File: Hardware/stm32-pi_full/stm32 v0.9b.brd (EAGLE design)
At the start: 131.4 x 105.8 mm, 272 parts, among them J1 SOLDERJUMPERNO, J2 5-1814400-1, U1 ESP32-WROOM-32D, Y1 6MM_3.5MM_CRYSTAL

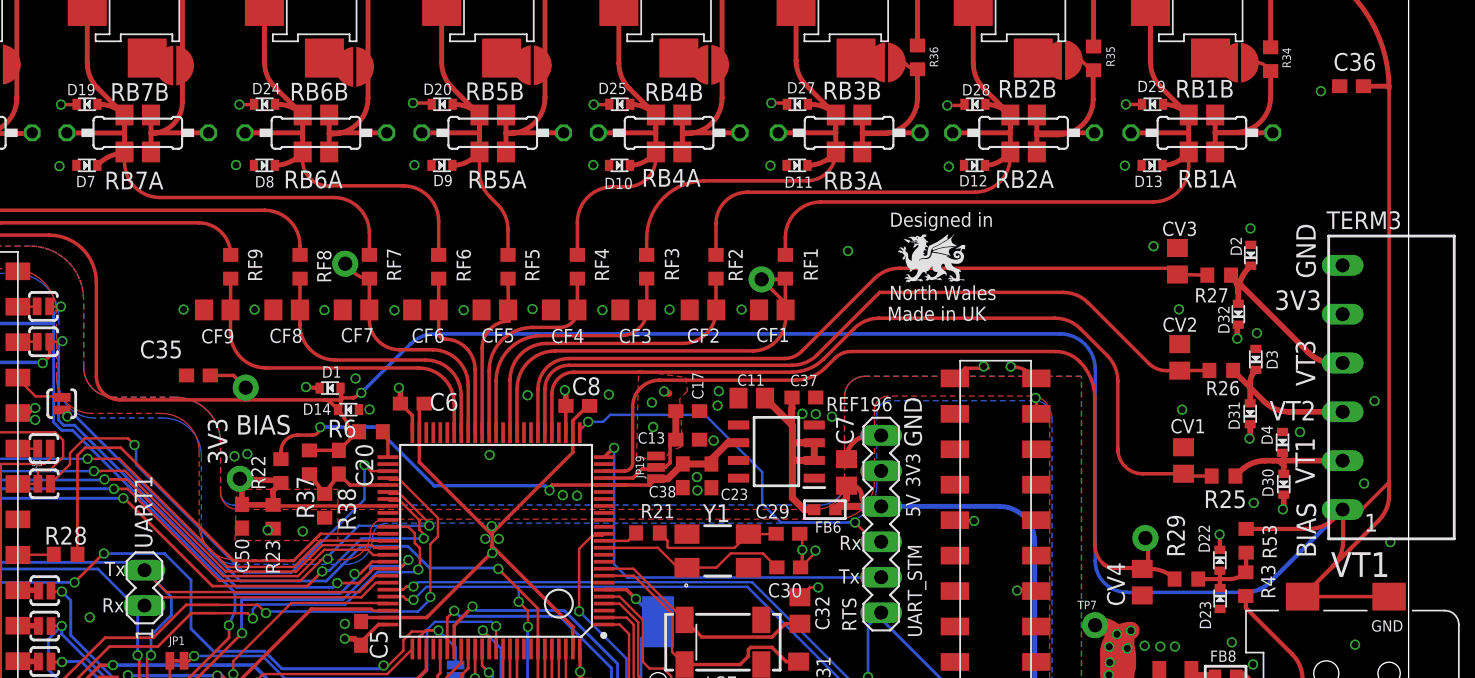
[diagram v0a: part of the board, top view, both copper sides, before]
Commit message: bias changed to inverting op-amp with in-the-loop compensator
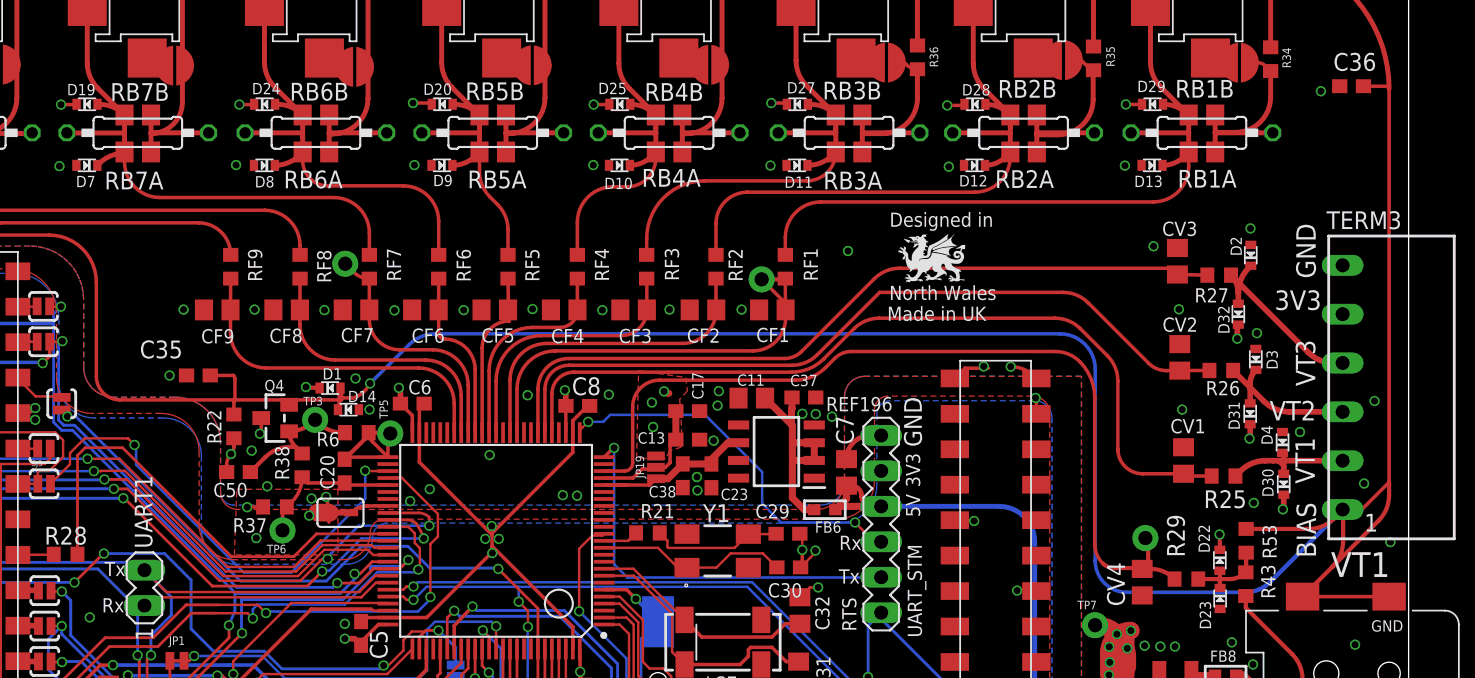
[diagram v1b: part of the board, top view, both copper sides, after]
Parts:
- removed R23: 10k, resistor:R0603
- removed TP10: TEST-POINTPOGO_PTH, SparkFun-Connectors:1X01_NO_SILK
- added Q4: (no value), microbuilder:SOT23-WIDE
- added SJ1: (no value), jumper-con_db:SJ-CON
- added TP3, TP6: TEST-POINTPOGO_PTH, SparkFun-Connectors:1X01_NO_SILK
- C20: value 2.2uF -> 2nF
- C50: value (none) -> 1nF
- R22: value 10k -> 1k
- R37: value 0R -> 1k
- R6: value 0R -> 5R
- moved TP5 10.9 mm to (58.4, 64.1)
- moved R22 4.65 mm to (47.2, 64.6)
- moved R37 4.04 mm to (50.2, 58.8), turned to 0 degrees
- moved R38 3.32 mm to (52.1, 61.8)
- moved C50 3.18 mm to (47.5, 61.3), turned to 180 degrees
- moved R6 1.02 mm to (56.0, 64.1), turned to 180 degrees
- moved C20 0.76 mm to (55.1, 61.4), turned to 90 degrees
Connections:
- removed net BIAS_: R6.2, STM32F303VE.51
- removed net BIAS_IN: C50.2, R22.1, R23.2, STM32F303VE.58, TP10.1
- new net OPAMP_FB2: C50.1, Q4.1, R38.1, R6.2, TP3.1
- new net OPAMP_NON-INVERT+: SJ1.1, STM32F303VE.58
- new net OPAMP_OUT: C20.2, R6.1, STM32F303VE.51, TP5.1
- net +3V3ANA: now also Q4.3, R37.1
- net AGND: now also C50.2, R22.1, SJ1.2; no longer C50.1, R23.1, R38.2
- net BIAS: now also Q4.2, R22.2; no longer C20.1, R37.1, R6.1, TP5.1
- net LED2: now also STM32F303VE.59; no longer STM32F303VE.56
- net LED3: now also STM32F303VE.60; no longer STM32F303VE.57
- net OPAMP_INVERT-: now also C20.1, R38.2, TP6.1; no longer C20.2, R38.1
- net VREF+: no longer R22.2
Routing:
- net VREF+: track 44.2 -> 12.7 mm, vias 2 -> 0
- net BIAS_IN: track 17.3 -> 0.00 mm
- net OPAMP_OUT: track 0.00 -> 11.3 mm
- net OPAMP_FB2: track 0.00 -> 10.1 mm
- net BIAS: track 577.6 -> 570.6 mm
- net AGND: track 15.5 -> 21.4 mm, vias 85 -> 91
- net OPAMP_INVERT-: track 7.39 -> 10.5 mm
- net OPAMP_NON-INVERT+: track 0.00 -> 2.74 mm
- net +3V3ANA: track 72.6 -> 74.9 mm, vias 23 -> 25
- net BIAS_: track 1.97 -> 0.00 mm
- net RPI_PWR: track 35.1 -> 33.5 mm
- net LED3: track 73.8 -> 73.0 mm
- net BUTTON1_STM: track 35.6 -> 35.0 mm

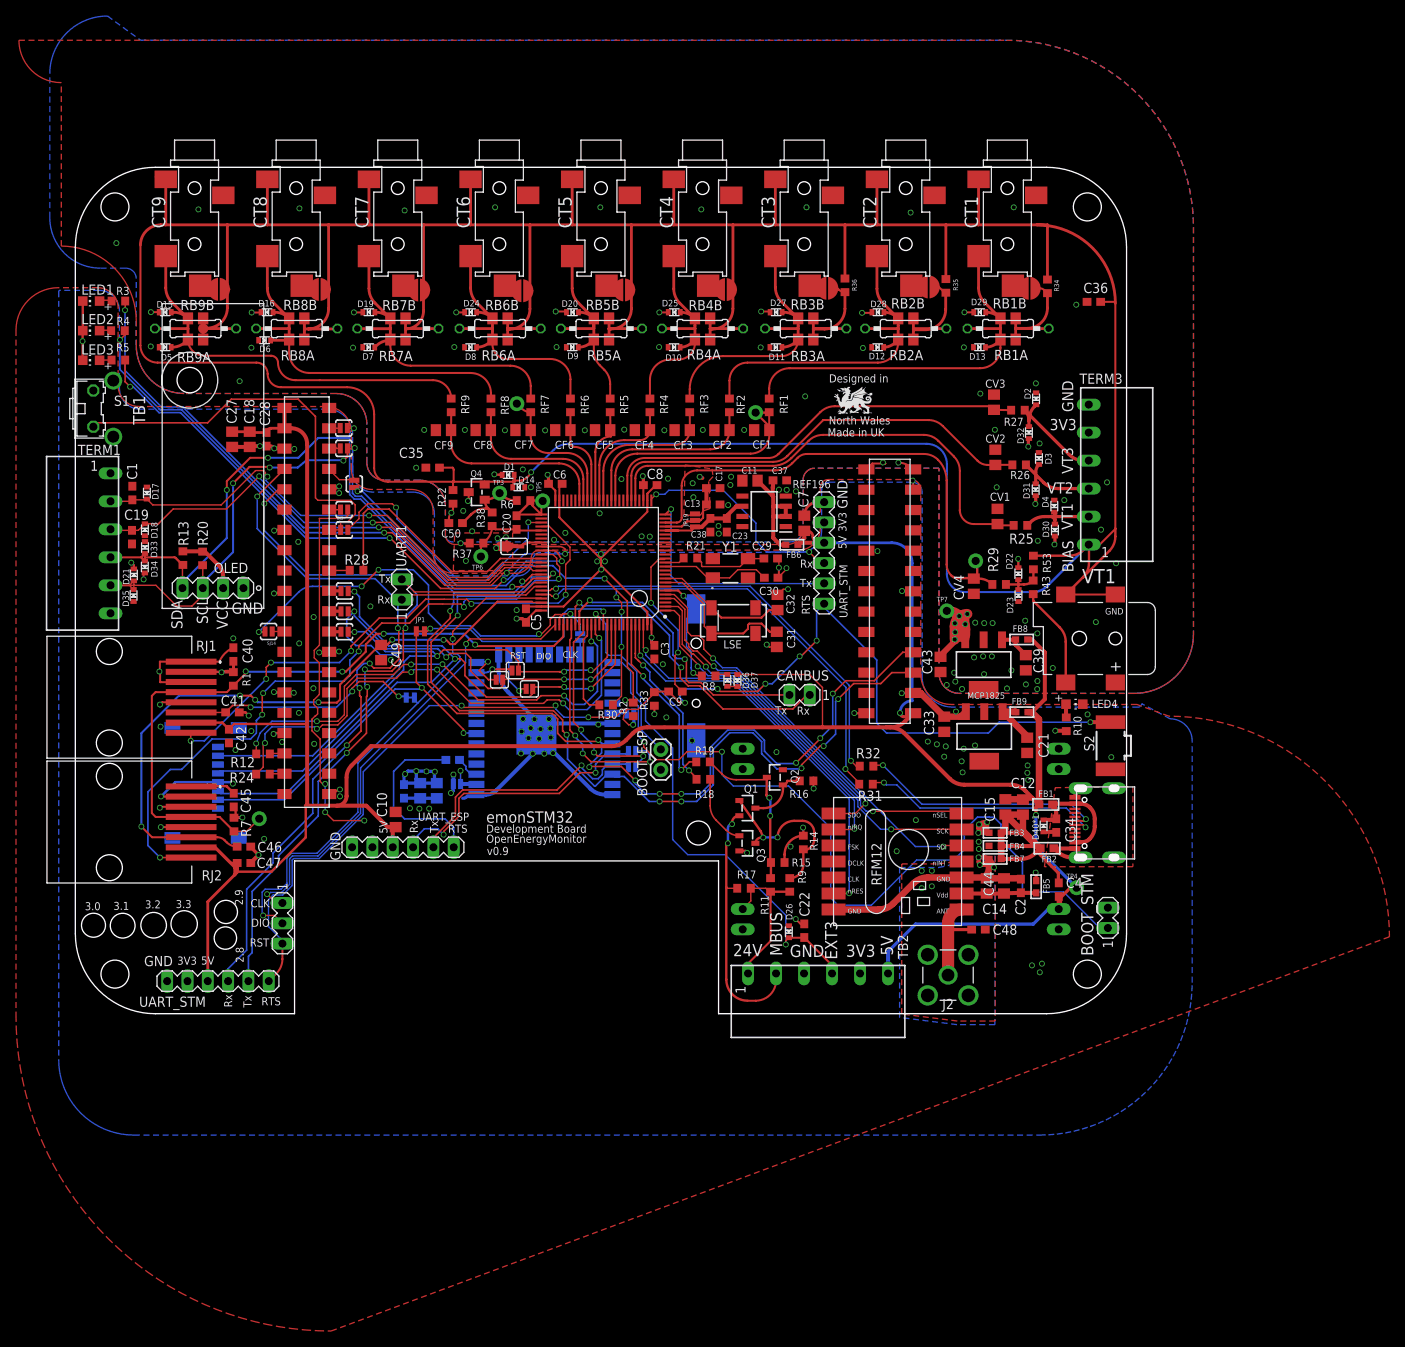
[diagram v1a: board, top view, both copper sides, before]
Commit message: update readme.md
including link for the enclosure CAD
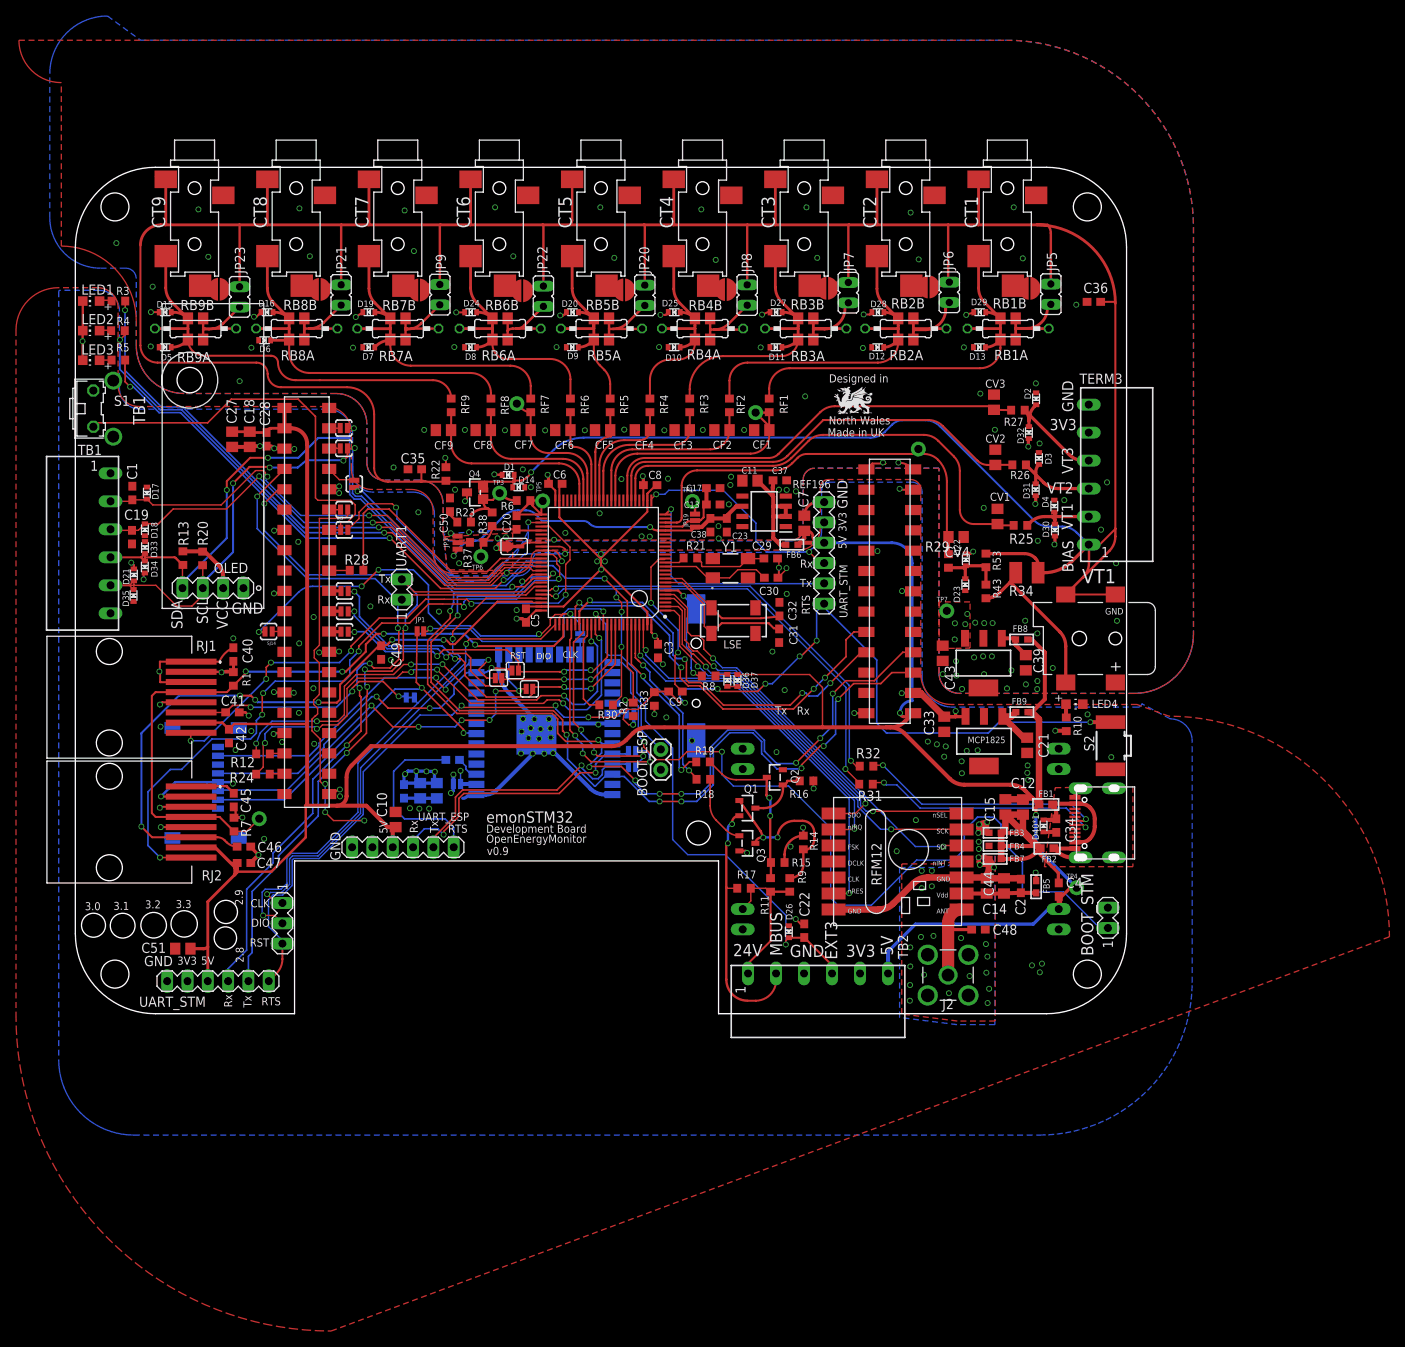
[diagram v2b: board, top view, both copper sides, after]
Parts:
- removed CANBUS: TX/RX, con-lstb-db:MA02-1
- removed R35, R36: 0R, rcl:R0603
- added C51: 22uF, rcl:C0805
- added JP2: JUMPER-SMT_2_NO_NO-SILK, SparkFun-Jumpers:SMT-JUMPER_2_NO_NO-SILK
- added JP20, JP21, JP22, JP23, JP5, JP6, JP7, JP8, JP9: (no value), jumper-con_db:JP1
- added JP3: JUMPER-SMT_3_NO_NO-SILK, SparkFun-Jumpers:SMT-JUMPER_3_NO_NO-SILK
- added R23: 1k, resistor:R0603
- added TP1: TEST-POINTPOGO_PTH, SparkFun-Connectors:1X01_NO_SILK
- C20: value 2nF -> 2.2nF
- C31, C32: device rcl:C0805 -> rcl:C0603
- C48: value 100nF -> (none)
- C49: value 10pF -> 1nF; device rcl:C0805 -> rcl:C0603
- C50: value 1nF -> 1uf
- C7: value 2.2uF -> 22uF
- CF1, CF2, CF3, CF4, CF5, CF6, CF7, CF8, CF9, CV1, CV2, CV3, CV4: value 10nF -> 10nF 5%
- JP1: value JUMPER-SMT_2_NC_TRACE_NO-SILK -> JUMPER-SMT_2_NO_NO-SILK; device SparkFun-Jumpers:SMT-JUMPER_2_NC_TRACE_NO-SILK -> SparkFun-Jumpers:SMT-JUMPER_2_NO_NO-SILK
- PS1: value LT1461AIS8-3.3#PBF -> REF191ESZ
- R22: value 1k -> 10k
- R25, R26, R27: value 9k1 -> 9k1 0.1%
- R34: value 0R -> (none); device rcl:R0603 -> rcl:R1210
- R37: value 1k -> 2k
- R6: value 5R -> 20R
- RB1A, RB1B: value 22r 0.3W 1% -> 22r
- RB1_: value 22r 0.5W -> (none)
- RB2_, RB3_, RB4_, RB5_, RB6_, RB7_, RB8_: value 22r -> (none)
- RB9A, RB9B: value 100R 0.1% -> 22r
- RB9_: value 100R 0.1% -> (none)
- moved R34 35.9 mm to (118.9, 55.1), turned to 0 degrees
- moved TP20 15.7 mm to (105.4, 70.6)
- moved R29 6.99 mm to (109.1, 56.6), turned to 90 degrees
- moved D22 6.79 mm to (111.3, 56.7)
- moved D23 6.79 mm to (111.2, 53.6)
- moved CV4 6.54 mm to (110.1, 59.6), turned to 0 degrees
- moved R53 5.94 mm to (113.8, 56.7)
- moved R43 5.93 mm to (113.8, 52.8)
- moved R22 3.00 mm to (46.3, 67.5), turned to 270 degrees
- moved C50 2.40 mm to (46.8, 63.6), turned to 90 degrees
- moved C35 2.24 mm to (42.4, 68.1)
- moved C43 1.42 mm to (108.4, 45.1)
- moved C32 0.87 mm to (88.0, 50.6)
- moved MCP1825 0.60 mm to (113.6, 34.1)
- moved C31 0.54 mm to (88.0, 47.2)
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- renumbered TERM1 to TB1
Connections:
- removed net IO3_EX: EXPANSION.17
- removed net IO5_EX: EXPANSION.19
- removed net N$28: JP14.1, R36.1, RB3A.2, RB3B.2, RB3_.2
- new net N$12: JP3.2, R37.1
- new net N$24: JP20.2, RB5A.2, RB5B.2, RB5_.2
- new net N$25: JP22.2, RB6A.2, RB6B.2, RB6_.2
- new net N$29: JP21.2, RB8A.2, RB8B.2, RB8_.2
- new net N$34: JP23.2, RB9A.2, RB9B.2, RB9_.2
- new net N$35: JP8.2, RB4A.2, RB4B.2, RB4_.2
- new net N$36: JP9.2, RB7A.2, RB7B.2, RB7_.2
- new net N$37: JP7.2, RB3A.2, RB3B.2, RB3_.2
- new net N$7: C50.1, R23.1
- net +3V3ANA: now also JP3.3, TP1.1; no longer R37.1
- net +5V: now also C51.1
- net AC1: now also R34.1
- net BIAS: now also JP10.1, JP12.1, JP14.1, JP2.2, JP20.1, JP21.1, JP22.1, JP23.1, JP5.1, JP6.1, JP7.1, JP8.1, JP9.1; no longer R35.2, R36.2, RB4A.2, RB4B.2, RB4_.2, RB5A.2, RB5B.2, RB5_.2, RB6A.2, RB6B.2, RB6_.2, RB7A.2, RB7B.2, RB7_.2, RB8A.2, RB8B.2, RB8_.2, RB9A.2, RB9B.2, RB9_.2
- net CAN_RX: now also EXPANSION.17; no longer CANBUS.1
- net CAN_TX: now also EXPANSION.19; no longer CANBUS.2
- net DGND: now also C51.2
- net HSPI_CLK: now also U$7.PIN5
- net HSPI_ID/MOSI: now also U$7.PIN3
- net HSPI_Q/MISO: now also U$7.PIN7
- net N$26: now also JP5.2; no longer JP10.1, R34.1
- net N$27: now also JP6.2; no longer JP12.1, R35.1
- net OPAMP_FB2: now also JP2.1, R23.2; no longer C50.1
- net SPI1_CLK_SLAVE: no longer U$7.PIN5
- net SPI1_MISO_SLAVE: no longer U$7.PIN7
- net SPI1_MOSI_SLAVE: no longer U$7.PIN3
- net VREF+: now also JP3.1
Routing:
- net BIAS: track 570.6 -> 499.3 mm
- net HSPI_ID/MOSI: track 6.21 -> 52.9 mm, vias 1 -> 6
- net SPI1_MISO_SLAVE: track 84.8 -> 45.0 mm
- net HSPI_CLK: track 4.57 -> 44.3 mm, vias 1 -> 3
- net HSPI_Q/MISO: track 5.65 -> 44.9 mm, vias 1 -> 3
- net SPI1_MOSI_SLAVE: track 85.9 -> 49.0 mm
- net SPI1_CLK_SLAVE: track 75.5 -> 41.4 mm
- net +3V3ANA: track 74.9 -> 44.9 mm, vias 25 -> 20
- net VREF+: track 12.7 -> 41.2 mm, vias 0 -> 2
- net N$28: track 14.9 -> 0.00 mm
- net CAN_TX: track 36.5 -> 49.6 mm, vias 2 -> 4
- net N$37: track 0.00 -> 12.9 mm
- net N$34: track 0.00 -> 12.3 mm
- net N$36: track 0.00 -> 12.2 mm
- net AC1: track 12.6 -> 24.7 mm
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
